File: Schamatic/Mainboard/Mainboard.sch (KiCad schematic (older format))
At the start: 73 parts, among them J1 CONN_01X02, J2 CONN_01X02, J3 CONN_01X02, J4 CONN_01X02, J5 CONN_01X02, J6 CONN_02X05, J7 CONN_02X20, J8 CONN_01X02, J9 CONN_01X02, Q1 Q_NMOS_GDS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

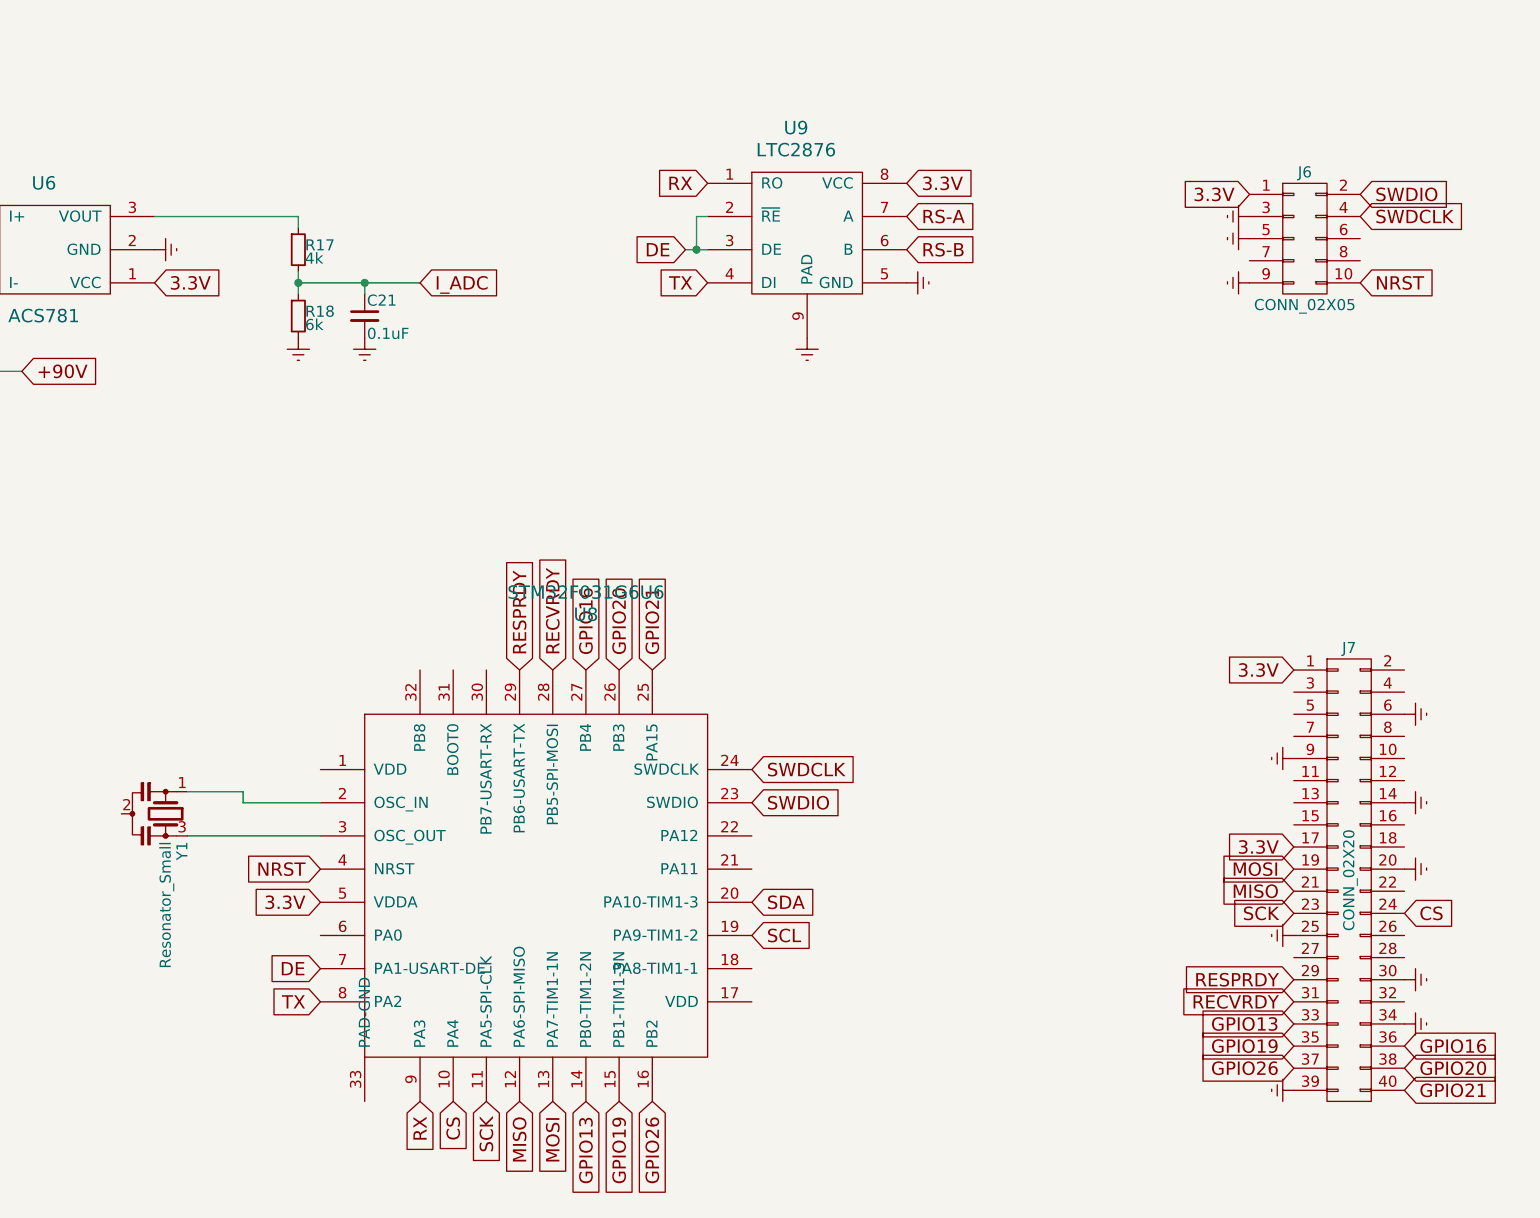
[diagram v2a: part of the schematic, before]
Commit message: 3d updates for new controller
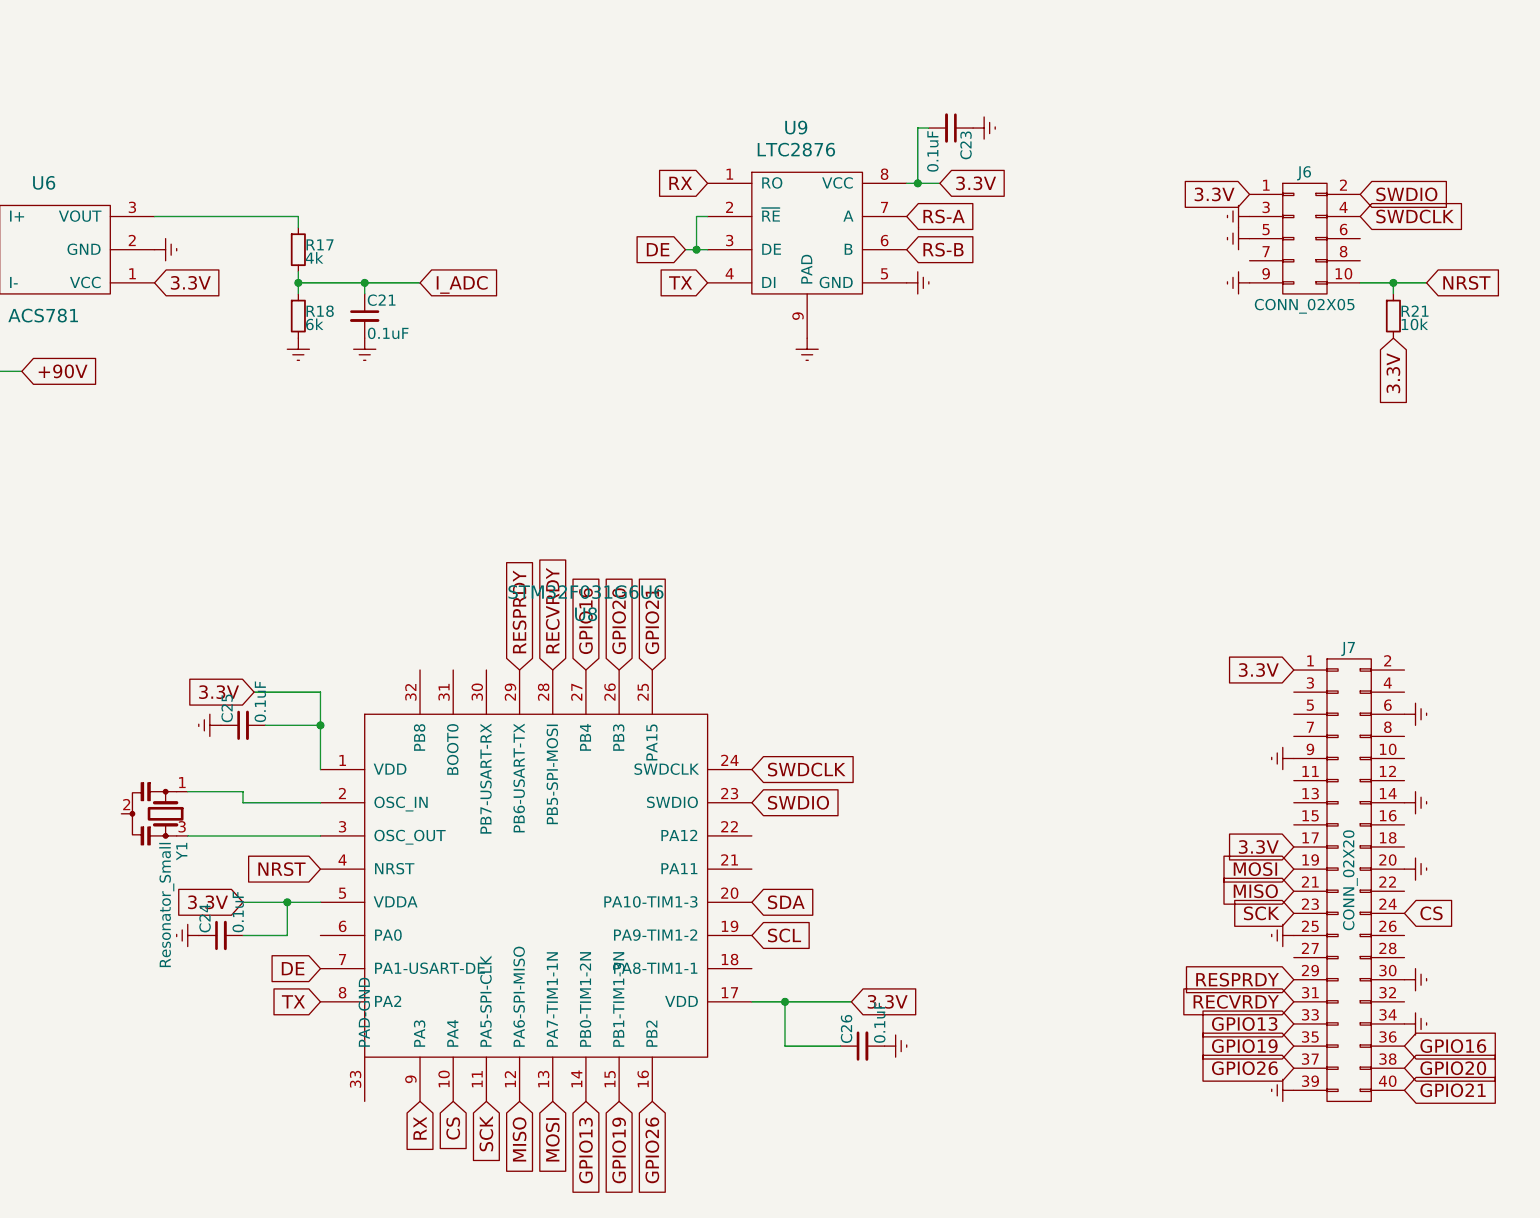
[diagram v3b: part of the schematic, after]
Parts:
- added C23, C24, C25, C26: 0.1uF, Capacitors_SMD:C_0603, symbol C_Small
- added R21: 10k, Resistors_SMD:R_0603, symbol R_Small
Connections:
- net 3.3V: now also U8.1 (VDD), U8.17 (VDD), C23.2, C24.2, C25.2, C26.1, R21.2
- net Earth: now also C23.1, C24.1, C25.1, C26.2
- net NRST: now also R21.1
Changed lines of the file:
@@
 $EndComp
 $Comp
-L Earth #PWR46
+L Earth #PWR48
 U 1 1 5B26D2B1
 P 9500 2100
-F 0 "#PWR46" H 9500 1850 50  0001 C CNN
+F 0 "#PWR48" H 9500 1850 50  0001 C CNN
 F 1 "Earth" H 9500 1950 50  0001 C CNN
 F 2 "" H 9500 2100 50  0001 C CNN
@@
 $EndComp
 $Comp
-L Earth #PWR47
+L Earth #PWR49
 U 1 1 5B26D322
 P 9800 2100
-F 0 "#PWR47" H 9800 1850 50  0001 C CNN
+F 0 "#PWR49" H 9800 1850 50  0001 C CNN
 F 1 "Earth" H 9800 1950 50  0001 C CNN
 F 2 "" H 9800 2100 50  0001 C CNN
@@
 Connection ~ 9100 7550
 $Comp
-L Earth #PWR45
+L Earth #PWR47
 U 1 1 5B26DBCC
 P 9450 7700
-F 0 "#PWR45" H 9450 7450 50  0001 C CNN
+F 0 "#PWR47" H 9450 7450 50  0001 C CNN
 F 1 "Earth" H 9450 7550 50  0001 C CNN
 F 2 "" H 9450 7700 50  0001 C CNN
@@
 3.3V
 $Comp
-L Earth #PWR54
+L Earth #PWR58
 U 1 1 5B2B960D
 P 13800 1550
-F 0 "#PWR54" H 13800 1300 50  0001 C CNN
+F 0 "#PWR58" H 13800 1300 50  0001 C CNN
 F 1 "Earth" H 13800 1400 50  0001 C CNN
 F 2 "" H 13800 1550 50  0001 C CNN
@@
 $EndComp
 $Comp
-L Earth #PWR55
+L Earth #PWR59
 U 1 1 5B2B9CE4
 P 13800 1650
-F 0 "#PWR55" H 13800 1400 50  0001 C CNN
+F 0 "#PWR59" H 13800 1400 50  0001 C CNN
 F 1 "Earth" H 13800 1500 50  0001 C CNN
 F 2 "" H 13800 1650 50  0001 C CNN
@@
 $EndComp
 $Comp
-L Earth #PWR56
+L Earth #PWR60
 U 1 1 5B2B9DA3
 P 13800 1850
-F 0 "#PWR56" H 13800 1600 50  0001 C CNN
+F 0 "#PWR60" H 13800 1600 50  0001 C CNN
 F 1 "Earth" H 13800 1700 50  0001 C CNN
 F 2 "" H 13800 1850 50  0001 C CNN
@@
 Text GLabel 14300 1550 2    60   Input ~ 0
 SWDCLK
-Text GLabel 14300 1850 2    60   Input ~ 0
+Text GLabel 14600 1850 2    60   Input ~ 0
 NRST
 $Comp
@@
 Text GLabel 11350 1850 0    60   Input ~ 0
 TX
-Text GLabel 12250 1400 2    60   Input ~ 0
+Text GLabel 12400 1400 2    60   Input ~ 0
 3.3V
 Text GLabel 12250 1550 2    60   Input ~ 0
@@
 RS-B
 $Comp
-L Earth #PWR51
+L Earth #PWR54
 U 1 1 5B2BC8D0
 P 12250 1850
-F 0 "#PWR51" H 12250 1600 50  0001 C CNN
+F 0 "#PWR54" H 12250 1600 50  0001 C CNN
 F 1 "Earth" H 12250 1700 50  0001 C CNN
 F 2 "" H 12250 1850 50  0001 C CNN
@@
 $EndComp
 $Comp
-L Earth #PWR48
+L Earth #PWR50
 U 1 1 5B2BD03E
 P 11800 2100
-F 0 "#PWR48" H 11800 1850 50  0001 C CNN
+F 0 "#PWR50" H 11800 1850 50  0001 C CNN
 F 1 "Earth" H 11800 1950 50  0001 C CNN
 F 2 "" H 11800 2100 50  0001 C CNN
@@
 Text GLabel 9600 4500 0    60   Input ~ 0
 NRST
-Text GLabel 9600 4650 0    60   Input ~ 0
+Text GLabel 9250 4650 0    60   Input ~ 0
 3.3V
 Text GLabel 9600 4950 0    60   Input ~ 0
@@
 $EndComp
 $Comp
-L Earth #PWR52
+L Earth #PWR56
 U 1 1 5B2C9857
 P 12600 7400
-F 0 "#PWR52" H 12600 7150 50  0001 C CNN
+F 0 "#PWR56" H 12600 7150 50  0001 C CNN
 F 1 "Earth" H 12600 7250 50  0001 C CNN
 F 2 "" H 12600 7400 50  0001 C CNN
@@
 $EndComp
 $Comp
-L Earth #PWR53
+L Earth #PWR57
 U 1 1 5B2C9D94
 P 12600 7750
-F 0 "#PWR53" H 12600 7500 50  0001 C CNN
+F 0 "#PWR57" H 12600 7500 50  0001 C CNN
 F 1 "Earth" H 12600 7600 50  0001 C CNN
 F 2 "" H 12600 7750 50  0001 C CNN
@@
 3.3V
 $Comp
-L Earth #PWR64
+L Earth #PWR68
 U 1 1 5B2CEE98
 P 14500 3800
-F 0 "#PWR64" H 14500 3550 50  0001 C CNN
+F 0 "#PWR68" H 14500 3550 50  0001 C CNN
 F 1 "Earth" H 14500 3650 50  0001 C CNN
 F 2 "" H 14500 3800 50  0001 C CNN
@@
 $EndComp
 $Comp
-L Earth #PWR57
+L Earth #PWR61
 U 1 1 5B2CF2D3
 P 14000 4000
-F 0 "#PWR57" H 14000 3750 50  0001 C CNN
+F 0 "#PWR61" H 14000 3750 50  0001 C CNN
 F 1 "Earth" H 14000 3850 50  0001 C CNN
 F 2 "" H 14000 4000 50  0001 C CNN
@@
 SCK
 $Comp
-L Earth #PWR58
+L Earth #PWR62
 U 1 1 5B2D0DDB
 P 14000 4800
-F 0 "#PWR58" H 14000 4550 50  0001 C CNN
+F 0 "#PWR62" H 14000 4550 50  0001 C CNN
 F 1 "Earth" H 14000 4650 50  0001 C CNN
 F 2 "" H 14000 4800 50  0001 C CNN
@@
 $EndComp
 $Comp
-L Earth #PWR59
+L Earth #PWR63
 U 1 1 5B2D1084
 P 14000 5500
-F 0 "#PWR59" H 14000 5250 50  0001 C CNN
+F 0 "#PWR63" H 14000 5250 50  0001 C CNN
 F 1 "Earth" H 14000 5350 50  0001 C CNN
 F 2 "" H 14000 5500 50  0001 C CNN
@@
 $EndComp
 $Comp
-L Earth #PWR65
+L Earth #PWR69
 U 1 1 5B2D1158
 P 14500 4200
-F 0 "#PWR65" H 14500 3950 50  0001 C CNN
+F 0 "#PWR69" H 14500 3950 50  0001 C CNN
 F 1 "Earth" H 14500 4050 50  0001 C CNN
 F 2 "" H 14500 4200 50  0001 C CNN
@@
 $EndComp
 $Comp
-L Earth #PWR66
+L Earth #PWR70
 U 1 1 5B2D122C
 P 14500 4500
-F 0 "#PWR66" H 14500 4250 50  0001 C CNN
+F 0 "#PWR70" H 14500 4250 50  0001 C CNN
 F 1 "Earth" H 14500 4350 50  0001 C CNN
 F 2 "" H 14500 4500 50  0001 C CNN
@@
 $EndComp
 $Comp
-L Earth #PWR67
+L Earth #PWR71
 U 1 1 5B2D1300
 P 14500 5000
-F 0 "#PWR67" H 14500 4750 50  0001 C CNN
+F 0 "#PWR71" H 14500 4750 50  0001 C CNN
 F 1 "Earth" H 14500 4850 50  0001 C CNN
 F 2 "" H 14500 5000 50  0001 C CNN
@@
 $EndComp
 $Comp
-L Earth #PWR68
+L Earth #PWR72
 U 1 1 5B2D13D4
 P 14500 5200
-F 0 "#PWR68" H 14500 4950 50  0001 C CNN
+F 0 "#PWR72" H 14500 4950 50  0001 C CNN
 F 1 "Earth" H 14500 5050 50  0001 C CNN
 F 2 "" H 14500 5200 50  0001 C CNN
@@
 $EndComp
 $Comp
-L +BATT #PWR60
+L +BATT #PWR64
 U 1 1 5B2D9D20
 P 14050 7650
-F 0 "#PWR60" H 14050 7500 50  0001 C CNN
+F 0 "#PWR64" H 14050 7500 50  0001 C CNN
 F 1 "+BATT" H 14050 7790 50  0000 C CNN
 F 2 "" H 14050 7650 50  0001 C CNN
@@
 $EndComp
 $Comp
-L Earth #PWR61
+L Earth #PWR65
 U 1 1 5B2DAAD7
 P 14050 7750
-F 0 "#PWR61" H 14050 7500 50  0001 C CNN
+F 0 "#PWR65" H 14050 7500 50  0001 C CNN
 F 1 "Earth" H 14050 7600 50  0001 C CNN
 F 2 "" H 14050 7750 50  0001 C CNN
@@
 +90V
 $Comp
-L Earth #PWR62
+L Earth #PWR66
 U 1 1 5B2DF71F
 P 14050 8450
-F 0 "#PWR62" H 14050 8200 50  0001 C CNN
+F 0 "#PWR66" H 14050 8200 50  0001 C CNN
 F 1 "Earth" H 14050 8300 50  0001 C CNN
 F 2 "" H 14050 8450 50  0001 C CNN
@@
 +90V
 $Comp
-L Earth #PWR63
+L Earth #PWR67
 U 1 1 5B2DF811
 P 14050 8850
-F 0 "#PWR63" H 14050 8600 50  0001 C CNN
+F 0 "#PWR67" H 14050 8600 50  0001 C CNN
 F 1 "Earth" H 14050 8700 50  0001 C CNN
 F 2 "" H 14050 8850 50  0001 C CNN
@@
 $EndComp
 $Comp
-L Earth #PWR50
+L Earth #PWR53
 U 1 1 5B3020A0
 P 12150 8850
-F 0 "#PWR50" H 12150 8600 50  0001 C CNN
+F 0 "#PWR53" H 12150 8600 50  0001 C CNN
 F 1 "Earth" H 12150 8700 50  0001 C CNN
 F 2 "" H 12150 8850 50  0001 C CNN
@@
 $EndComp
 $Comp
-L Earth #PWR49
+L Earth #PWR52
 U 1 1 5B302186
 P 12150 8500
-F 0 "#PWR49" H 12150 8250 50  0001 C CNN
+F 0 "#PWR52" H 12150 8250 50  0001 C CNN
 F 1 "Earth" H 12150 8350 50  0001 C CNN
 F 2 "" H 12150 8500 50  0001 C CNN
@@
 Text GLabel 12150 8750 2    60   Input ~ 0
 5V
+$Comp
+L C_Small C23
+U 1 1 5B307AA3
+P 12450 1150
+F 0 "C23" H 12460 1220 50  0000 L CNN
+F 1 "0.1uF" H 12460 1070 50  0000 L CNN
+F 2 "Capacitors_SMD:C_0603" H 12450 1150 50  0001 C CNN
+F 3 "" H 12450 1150 50  0001 C CNN
+	1    12450 1150
+	0    1    1    0
+$EndComp
+Wire Wire Line
+	12400 1400 12250 1400
+Wire Wire Line
+	12350 1150 12300 1150
+Wire Wire Line
+	12300 1150 12300 1400
+Connection ~ 12300 1400
+$Comp
+L Earth #PWR55
+U 1 1 5B307E98
+P 12550 1150
+F 0 "#PWR55" H 12550 900 50  0001 C CNN
+F 1 "Earth" H 12550 1000 50  0001 C CNN
+F 2 "" H 12550 1150 50  0001 C CNN
+F 3 "" H 12550 1150 50  0001 C CNN
+	1    12550 1150
+	0    -1   -1   0
+$EndComp
+$Comp
+L R_Small R21
+U 1 1 5B30927A
+P 14450 2000
+F 0 "R21" H 14480 2020 50  0000 L CNN
+F 1 "10k" H 14480 1960 50  0000 L CNN
+F 2 "Resistors_SMD:R_0603" H 14450 2000 50  0001 C CNN
+F 3 "" H 14450 2000 50  0001 C CNN
+	1    14450 2000
+	1    0    0    -1
+$EndComp
+Wire Wire Line
+	14600 1850 14300 1850
+Wire Wire Line
+	14450 1900 14450 1850
+Connection ~ 14450 1850
+Text GLabel 14450 2100 3    60   Input ~ 0
+3.3V
+$Comp
+L C_Small C24
+U 1 1 5B30FD4E
+P 9150 4800
+F 0 "C24" H 9160 4870 50  0000 L CNN
+F 1 "0.1uF" H 9160 4720 50  0000 L CNN
+F 2 "Capacitors_SMD:C_0603" H 9150 4800 50  0001 C CNN
+F 3 "" H 9150 4800 50  0001 C CNN
+	1    9150 4800
+	0    -1   -1   0
+$EndComp
+$Comp
+L Earth #PWR45
+U 1 1 5B30FD54
+P 9050 4800
+F 0 "#PWR45" H 9050 4550 50  0001 C CNN
+F 1 "Earth" H 9050 4650 50  0001 C CNN
+F 2 "" H 9050 4800 50  0001 C CNN
+F 3 "" H 9050 4800 50  0001 C CNN
+	1    9050 4800
+	0    1    1    0
+$EndComp
+Wire Wire Line
+	9250 4650 9600 4650
+Wire Wire Line
+	9250 4800 9450 4800
+Wire Wire Line
+	9450 4800 9450 4650
+Connection ~ 9450 4650
+Text GLabel 12000 5100 2    60   Input ~ 0
+3.3V
+$Comp
+L C_Small C26
+U 1 1 5B3101CC
+P 12050 5300
+F 0 "C26" H 12060 5370 50  0000 L CNN
+F 1 "0.1uF" H 12060 5220 50  0000 L CNN
+F 2 "Capacitors_SMD:C_0603" H 12050 5300 50  0001 C CNN
+F 3 "" H 12050 5300 50  0001 C CNN
+	1    12050 5300
+	0    -1   -1   0
+$EndComp
+$Comp
+L Earth #PWR51
+U 1 1 5B3101D2
+P 12150 5300
+F 0 "#PWR51" H 12150 5050 50  0001 C CNN
+F 1 "Earth" H 12150 5150 50  0001 C CNN
+F 2 "" H 12150 5300 50  0001 C CNN
+F 3 "" H 12150 5300 50  0001 C CNN
+	1    12150 5300
+	0    -1   -1   0
+$EndComp
+Wire Wire Line
+	9600 4050 9600 3700
+Connection ~ 9600 3850
+Wire Wire Line
+	12000 5100 11550 5100
+Wire Wire Line
+	11950 5300 11700 5300
+Wire Wire Line
+	11700 5300 11700 5100
+Connection ~ 11700 5100
+Text GLabel 9300 3700 0    60   Input ~ 0
+3.3V
+$Comp
+L C_Small C25
+U 1 1 5B311BD4
+P 9250 3850
+F 0 "C25" H 9260 3920 50  0000 L CNN
+F 1 "0.1uF" H 9260 3770 50  0000 L CNN
+F 2 "Capacitors_SMD:C_0603" H 9250 3850 50  0001 C CNN
+F 3 "" H 9250 3850 50  0001 C CNN
+	1    9250 3850
+	0    -1   -1   0
+$EndComp
+$Comp
+L Earth #PWR46
+U 1 1 5B311CF4
+P 9150 3850
+F 0 "#PWR46" H 9150 3600 50  0001 C CNN
+F 1 "Earth" H 9150 3700 50  0001 C CNN
+F 2 "" H 9150 3850 50  0001 C CNN
+F 3 "" H 9150 3850 50  0001 C CNN
+	1    9150 3850
+	0    1    1    0
+$EndComp
+Wire Wire Line
+	9600 3700 9300 3700
+Wire Wire Line
+	9350 3850 9600 3850
 $EndSCHEMATC

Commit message: continue working on mainboard
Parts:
- added C27: 2.2uF, Capacitors_SMD:C_0603, symbol C_Small
- added J10: CONN_01X04, Pin_Headers:Pin_Header_Straight_1x04_Pitch2.54mm, symbol CONN_01X04
- added U10: LTC2954, Dizzy:8-DFN-DDB, symbol LTC2954
- R4: value 83k -> 10k
- R5: value 10k -> 390
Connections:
- net +BATT: now also U10.4 (VIN); no longer R4.1
- net 3.3V: now also R4.1, R5.2
- net Earth: now also C27.1, J10.1 (P1), J10.3 (P3), U10.1 (GND), U10.9 (PAD); no longer R5.2
- net GPIO16: now also J7.16 (P16), U8.26 (PB3)
- net I_ADC: now also U8.6 (PA0)
- net V_ADC: now also U8.14 (PB0-TIM1-2N)
- net at C9.2, D3.1 (K), U2.8 (VS): no longer U2.7 (EN)
- net at C10.2, D4.1 (K), U1.8 (VS): no longer U1.7 (EN)
- net GPIO18: now reaches J7.18 (P18)
- net GPIO18: now also U8.25 (PA15)
- net GPIO13: no longer names the net of J7.33 (P33)
- net GPIO13: no longer U8.14 (PB0-TIM1-2N)
- net GPIO20 renamed PWR_INT
- net PWR_INT: now also U10.8 (~INT); no longer U8.26 (PB3)
- net GPIO21 renamed ~PWR_KILL
- net ~PWR_KILL: now also R4.2, U10.5 (~KILL); no longer U8.25 (PA15)
- new net: C27.2, U10.6 (PDT)
- new net: J10.2 (P2), R5.1
- new net PWR_BUTTON: J10.4 (P4), U10.3 (~PB)
- new net PWR_EN: U1.7 (EN), U10.7 (~EN), U2.7 (EN), U4.6 (UVLO)
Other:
- moved on the sheet: C1, C24, R1
